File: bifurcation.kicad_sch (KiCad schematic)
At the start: 20 parts, among them J2 10061913-102PLF, J6 10061913-102PLF, U1 ZL40264LDG1

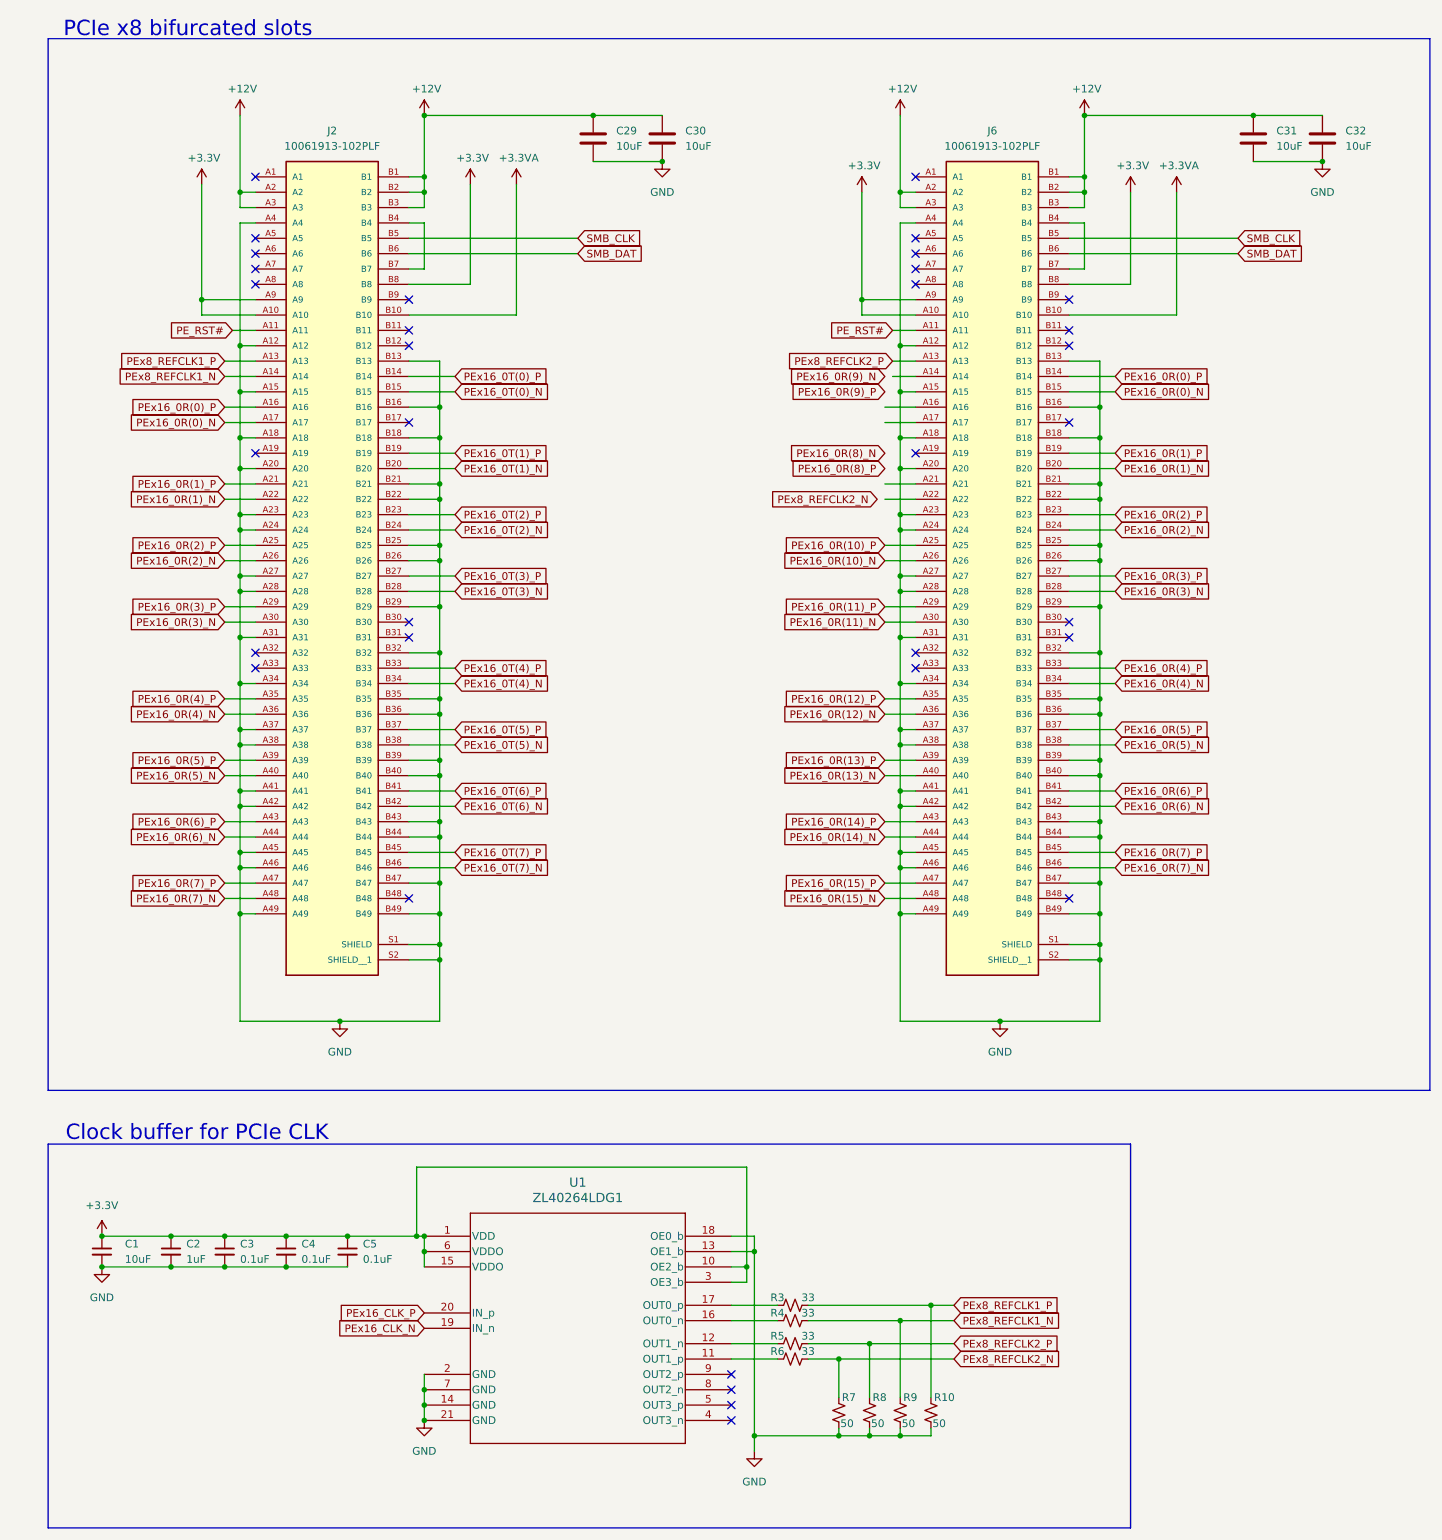
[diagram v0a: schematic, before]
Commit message: pcie traces routed
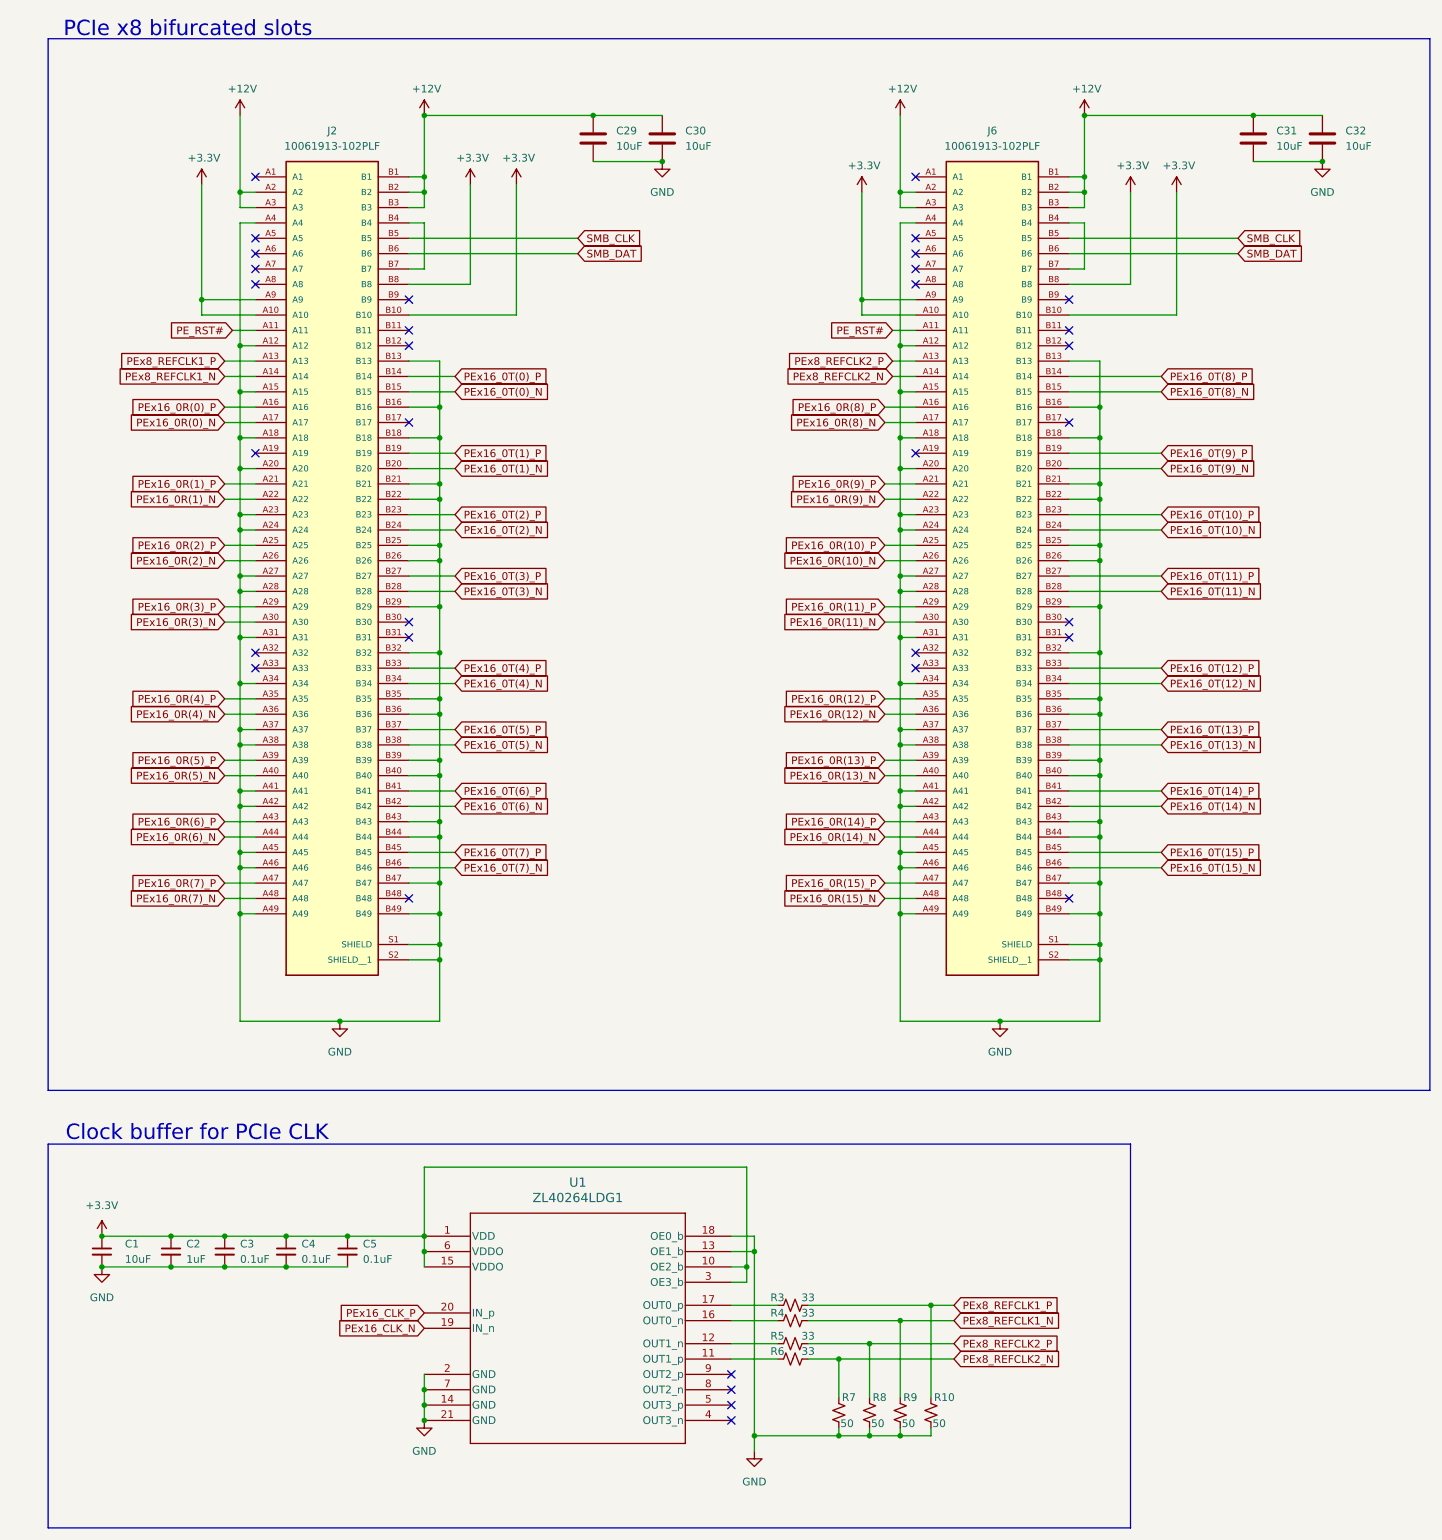
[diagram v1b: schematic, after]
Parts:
- C2, C3, C4, C5: footprint Capacitor_SMD:C_0201_0603Metric_Pad0.64x0.40mm_HandSolder -> Capacitor_SMD:C_0603_1608Metric
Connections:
- net +3.3VA is gone; now on net +3.3V: J2.B10, J6.B10
- net PEx16_0R(0)_N: no longer J6.B15
- net PEx16_0R(0)_P: no longer J6.B14
- net PEx16_0R(1)_N: no longer J6.B20
- net PEx16_0R(1)_P: no longer J6.B19
- net PEx16_0R(2)_N: no longer J6.B24
- net PEx16_0R(2)_P: no longer J6.B23
- net PEx16_0R(3)_N: no longer J6.B28
- net PEx16_0R(3)_P: no longer J6.B27
- net PEx16_0R(4)_N: no longer J6.B34
- net PEx16_0R(4)_P: no longer J6.B33
- net PEx16_0R(5)_N: no longer J6.B38
- net PEx16_0R(5)_P: no longer J6.B37
- net PEx16_0R(6)_N: no longer J6.B42
- net PEx16_0R(6)_P: no longer J6.B41
- net PEx16_0R(7)_N: no longer J6.B46
- net PEx16_0R(7)_P: no longer J6.B45
- net PEx16_0R(8)_N: now also J6.A17
- net PEx16_0R(8)_P: now also J6.A16
- net PEx16_0R(9)_N: now also J6.A22
- net PEx16_0R(9)_P: now also J6.A21
- net PEx8_REFCLK2_N: now also J6.A14
- new net PEx16_0T(10)_N: J6.B24
- new net PEx16_0T(10)_P: J6.B23
- new net PEx16_0T(11)_N: J6.B28
- new net PEx16_0T(11)_P: J6.B27
- new net PEx16_0T(12)_N: J6.B34
- new net PEx16_0T(12)_P: J6.B33
- new net PEx16_0T(13)_N: J6.B38
- new net PEx16_0T(13)_P: J6.B37
- new net PEx16_0T(14)_N: J6.B42
- new net PEx16_0T(14)_P: J6.B41
- new net PEx16_0T(15)_N: J6.B46
- new net PEx16_0T(15)_P: J6.B45
- new net PEx16_0T(8)_N: J6.B15
- new net PEx16_0T(8)_P: J6.B14
- new net PEx16_0T(9)_N: J6.B20
- new net PEx16_0T(9)_P: J6.B19

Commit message: layout done!!
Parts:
- C2, C3, C4, C5: footprint Capacitor_SMD:C_0603_1608Metric -> Capacitor_SMD:C_0402_1005Metric
- R10, R3, R4, R5, R6, R7, R8, R9: footprint Resistor_SMD:R_0603_1608Metric_Pad0.98x0.95mm_HandSolder -> Resistor_SMD:R_0402_1005Metric
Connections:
- net GND: now also J2.B4, J2.B7, J6.B4, J6.B7
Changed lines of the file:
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@@
 	)
 	(junction
+		(at 191.77 73.66)
+		(diameter 0)
+		(color 0 0 0 0)
+	)
+	(junction
 		(at 158.75 232.41)
 		(diameter 0)
@@
 	)
 	(junction
+		(at 82.55 58.42)
+		(diameter 0)
+		(color 0 0 0 0)
+	)
+	(junction
 		(at 80.01 248.92)
 		(diameter 0)
@@
 	)
 	(junction
+		(at 82.55 73.66)
+		(diameter 0)
+		(color 0 0 0 0)
+	)
+	(junction
 		(at 49.53 101.6)
 		(diameter 0)
@@
 	)
 	(junction
+		(at 191.77 58.42)
+		(diameter 0)
+		(color 0 0 0 0)
+	)
+	(junction
 		(at 191.77 104.14)
 		(diameter 0)
@@
 	(wire
 		(pts
+			(xy 191.77 58.42) (xy 191.77 73.66)
+		)
+		(stroke
+			(width 0)
+			(type default)
+		)
+	)
+	(wire
+		(pts
 			(xy 158.75 109.22) (xy 161.29 109.22)
 		)
@@
 	(wire
 		(pts
-			(xy 77.47 50.8) (xy 80.01 50.8)
+			(xy 77.47 50.8) (xy 82.55 50.8)
 		)
 		(stroke
@@
 	(wire
 		(pts
-			(xy 80.01 50.8) (xy 80.01 58.42)
+			(xy 82.55 50.8) (xy 82.55 58.42)
 		)
 		(stroke
@@
 	(wire
 		(pts
-			(xy 77.47 58.42) (xy 80.01 58.42)
+			(xy 77.47 58.42) (xy 82.55 58.42)
 		)
 		(stroke
@@
 	(wire
 		(pts
-			(xy 186.69 50.8) (xy 189.23 50.8)
+			(xy 186.69 50.8) (xy 191.77 50.8)
 		)
 		(stroke
@@
 	(wire
 		(pts
-			(xy 186.69 58.42) (xy 189.23 58.42)
+			(xy 186.69 58.42) (xy 191.77 58.42)
 		)
 		(stroke
@@
 	(wire
 		(pts
+			(xy 82.55 58.42) (xy 82.55 73.66)
+		)
+		(stroke
+			(width 0)
+			(type default)
+		)
+	)
+	(wire
+		(pts
 			(xy 186.69 129.54) (xy 191.77 129.54)
 		)
@@
 	(wire
 		(pts
-			(xy 189.23 50.8) (xy 189.23 58.42)
+			(xy 191.77 50.8) (xy 191.77 58.42)
 		)
 		(stroke
@@
 			)
 		)
-		(property "Footprint" "Resistor_SMD:R_0603_1608Metric_Pad0.98x0.95mm_HandSolder"
+		(property "Footprint" "Resistor_SMD:R_0402_1005Metric"
 			(at 140.97 232.41 0)
 			(effects
@@
 			)
 		)
-		(property "Footprint" "Capacitor_SMD:C_0603_1608Metric"
+		(property "Footprint" "Capacitor_SMD:C_0402_1005Metric"
 			(at 46.99 220.98 0)
 			(effects
@@
 			)
 		)
-		(property "Footprint" "Capacitor_SMD:C_0603_1608Metric"
+		(property "Footprint" "Capacitor_SMD:C_0402_1005Metric"
 			(at 57.15 220.98 0)
 			(effects
@@
 			)
 		)
-		(property "Footprint" "Capacitor_SMD:C_0603_1608Metric"
+		(property "Footprint" "Capacitor_SMD:C_0402_1005Metric"
 			(at 38.1 220.98 0)
 			(effects
@@
 			)
 		)
-		(property "Footprint" "Resistor_SMD:R_0603_1608Metric_Pad0.98x0.95mm_HandSolder"
+		(property "Footprint" "Resistor_SMD:R_0402_1005Metric"
 			(at 148.59 247.65 0)
 			(effects
@@
 			)
 		)
-		(property "Footprint" "Resistor_SMD:R_0603_1608Metric_Pad0.98x0.95mm_HandSolder"
+		(property "Footprint" "Resistor_SMD:R_0402_1005Metric"
 			(at 140.97 236.22 0)
 			(effects
@@
 			)
 		)
-		(property "Footprint" "Resistor_SMD:R_0603_1608Metric_Pad0.98x0.95mm_HandSolder"
+		(property "Footprint" "Resistor_SMD:R_0402_1005Metric"
 			(at 140.97 229.87 0)
 			(effects
@@
 			)
 		)
-		(property "Footprint" "Resistor_SMD:R_0603_1608Metric_Pad0.98x0.95mm_HandSolder"
+		(property "Footprint" "Resistor_SMD:R_0402_1005Metric"
 			(at 158.75 247.65 0)
 			(effects
@@
 			)
 		)
-		(property "Footprint" "Resistor_SMD:R_0603_1608Metric_Pad0.98x0.95mm_HandSolder"
+		(property "Footprint" "Resistor_SMD:R_0402_1005Metric"
 			(at 140.97 238.76 0)
 			(effects
@@
 			)
 		)
-		(property "Footprint" "Resistor_SMD:R_0603_1608Metric_Pad0.98x0.95mm_HandSolder"
+		(property "Footprint" "Resistor_SMD:R_0402_1005Metric"
 			(at 163.83 247.65 0)
 			(effects
@@
 			)
 		)
-		(property "Footprint" "Capacitor_SMD:C_0603_1608Metric"
+		(property "Footprint" "Capacitor_SMD:C_0402_1005Metric"
 			(at 67.31 220.98 0)
 			(effects
@@
 			)
 		)
-		(property "Footprint" "Resistor_SMD:R_0603_1608Metric_Pad0.98x0.95mm_HandSolder"
+		(property "Footprint" "Resistor_SMD:R_0402_1005Metric"
 			(at 153.67 247.65 0)
 			(effects
